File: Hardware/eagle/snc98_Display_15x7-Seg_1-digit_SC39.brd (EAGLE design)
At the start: 154.9 x 33.5 mm, 72 parts, among them M10 IRLML2244, M11 IRLML2244, M4 IRLML2244, M5 IRLML2244, M6 IRLML2244, M7 IRLML2244, M8 IRLML2244, M9 IRLML2244, X1 MICROMATCH-12, X2 MICROMATCH-14, X3 MICROMATCH-12, X4 MICROMATCH-14

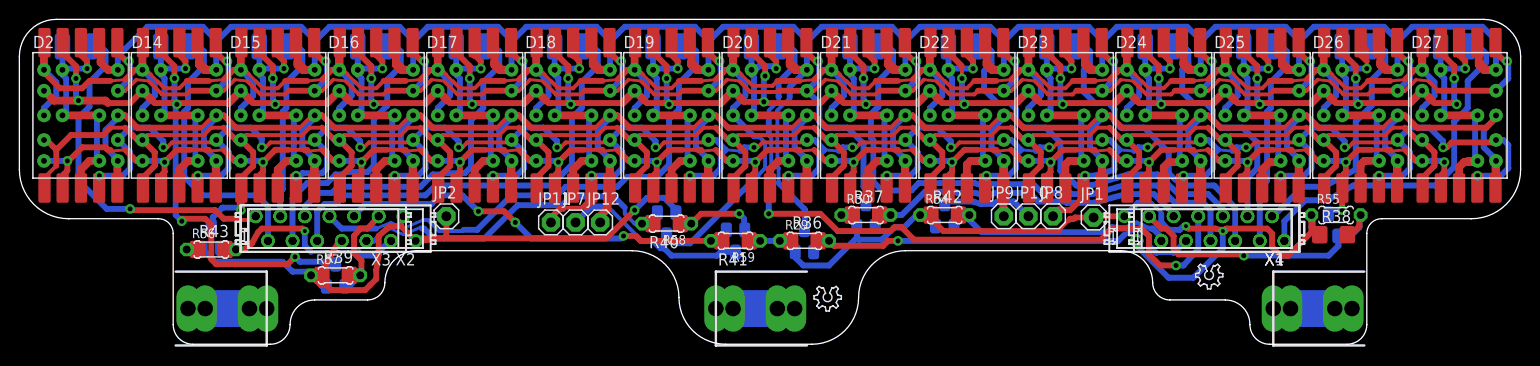
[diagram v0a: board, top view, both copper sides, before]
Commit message: PCB cleaning V1.1
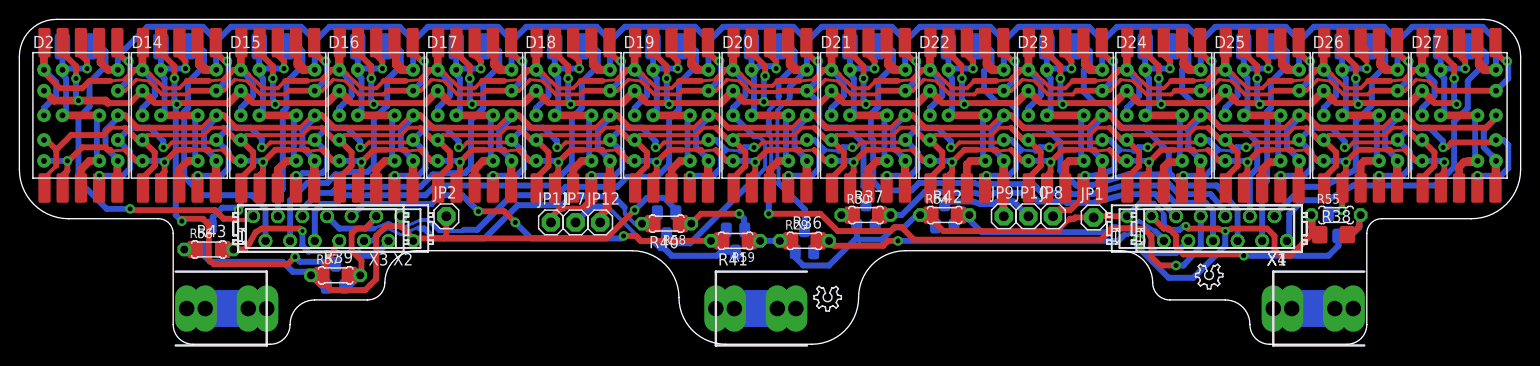
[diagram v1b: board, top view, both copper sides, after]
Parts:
- moved X1 0.25 mm to (123.8, 11.9)
- moved X2 0.25 mm to (32.4, 11.9)
- moved X4 0.25 mm to (122.6, 11.9)
- moved R43 0.25 mm to (19.6, 9.78)
- moved R56 0.25 mm to (19.6, 9.78)
- moved X3 0.25 mm to (31.1, 11.9)
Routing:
- net CA_LED: track 194.0 -> 193.3 mm

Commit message: PCB - add Tear Drop
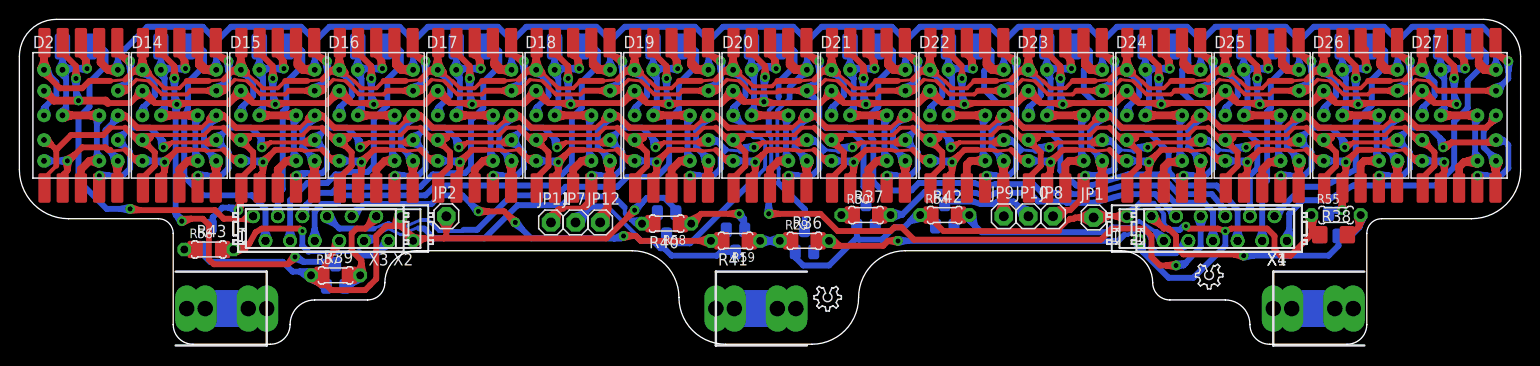
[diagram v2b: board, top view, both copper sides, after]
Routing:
- net SEG_F: track 306.5 -> 558.4 mm
- net SEG_C: track 294.2 -> 533.4 mm
- net SEG_DP: track 332.7 -> 540.6 mm
- net SEG_B: track 267.4 -> 447.4 mm
- net SEG_D: track 207.1 -> 387.0 mm
- net SEG_G: track 334.8 -> 493.4 mm
- net SEG_E: track 256.2 -> 381.6 mm
- net CA_LED: track 193.3 -> 302.3 mm
- net SEG_A: track 316.3 -> 376.4 mm
- net DIG_13: track 28.8 -> 57.5 mm
- net DIG_14: track 27.5 -> 56.0 mm
- net DIG_3: track 26.3 -> 52.5 mm
- net DIG_8: track 26.3 -> 52.5 mm
- net DIG_5: track 26.3 -> 52.5 mm
- net DIG_0: track 26.3 -> 52.5 mm
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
